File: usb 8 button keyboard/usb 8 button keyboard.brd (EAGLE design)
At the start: 108.5 x 37.8 mm, 31 parts, among them Q1 MMBT2222A, U1 ATMEGA32U4-AU, Y1 16MHZ

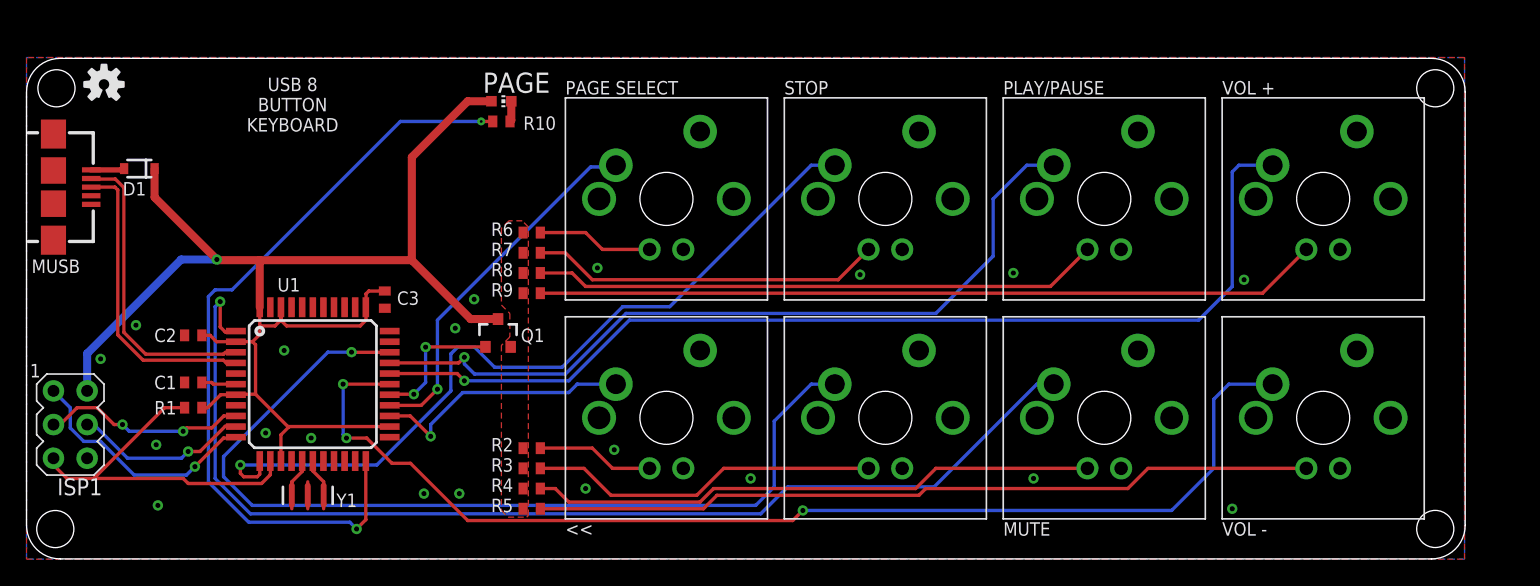
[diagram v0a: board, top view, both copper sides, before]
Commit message: add pcb with proper key spacing.
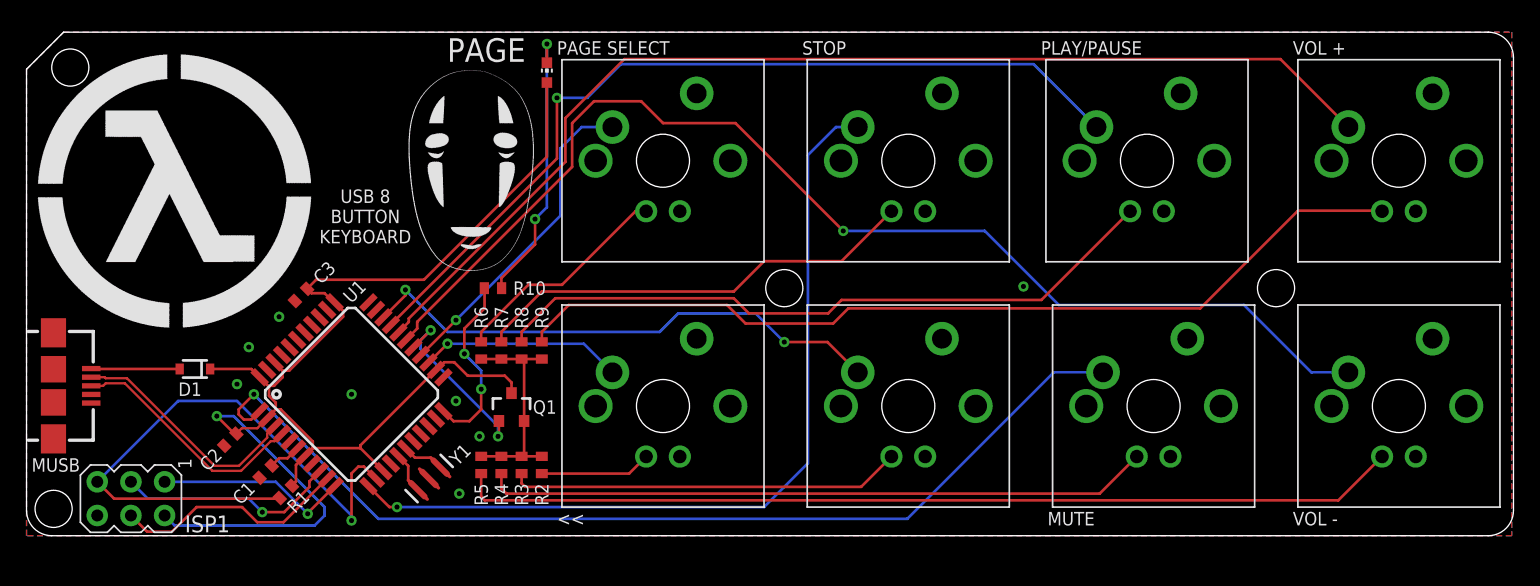
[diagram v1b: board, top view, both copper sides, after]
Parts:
- removed U$15: CPC1-3, cheeper:CPC1-3
- removed U$16: (no value), cheeper:CPC1-3
- moved U$1 81.4 mm to (80.7, 2.11), flipped to the bottom
- moved D1 15.7 mm to (12.7, 12.6)
- moved MUSB 15.0 mm to (2.03, 11.3)
- moved R10 12.6 mm to (35.2, 18.7)
- moved R6 9.67 mm to (34.3, 14.0), turned to 270 degrees
- moved R1 9.44 mm to (19.6, 3.30), turned to 225 degrees
- moved Y1 9.23 mm to (30.4, 4.32), turned to 225 degrees
- moved C1 8.67 mm to (18.0, 4.83), turned to 225 degrees
- moved C2 8.36 mm to (15.4, 7.24), turned to 225 degrees
- moved R7 7.71 mm to (35.8, 14.0), turned to 270 degrees
- moved ISP1 7.22 mm to (7.87, 2.79), turned to 270 degrees
- moved U$10 6.39 mm to (103.5, 28.3)
- moved C3 6.33 mm to (20.7, 18.2), turned to 225 degrees
- moved R8 5.89 mm to (37.3, 14.0), turned to 270 degrees
- moved U$9 5.78 mm to (103.5, 9.78)
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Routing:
- net PLED: track 58.9 -> 13.8 mm
- net SW1: track 71.0 -> 40.6 mm, vias 1 -> 2
- net N$3: track 1.57 -> 21.3 mm, vias 0 -> 2
- net RST: track 27.8 -> 45.9 mm, vias 0 -> 1
- net BL: track 0.00 -> 16.6 mm
- net N$11: track 59.0 -> 71.2 mm
- net N$15: track 59.1 -> 69.1 mm
- net SW2: track 85.2 -> 76.5 mm
- net N$14: track 42.8 -> 51.4 mm
- net N$12: track 8.77 -> 17.0 mm
- net N$10: track 42.7 -> 50.4 mm
- net N$13: track 26.5 -> 33.9 mm
- net SW5: track 60.1 -> 66.0 mm
- net SW4: track 78.6 -> 84.4 mm, vias 1 -> 0
- net D_N: track 22.9 -> 18.0 mm
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- removed copper zone on layer 1, net BL
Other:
- board size 108.5 x 37.8 mm -> 112.1 x 38 mm
- board text added: "C:/Users/Scott/Downloads/oZZuh.bmp"

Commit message: should be the right size now.
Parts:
- moved U$1 79.1 mm to (2.16, 11.3), turned to 270 degrees
- moved U$10 1.58 mm to (105.0, 28.8)
- moved U$11 1.58 mm to (86.0, 28.8)
- moved U$9 1.50 mm to (105.0, 9.78)
- moved U$8 1.00 mm to (86.0, 9.78)
- moved U$12 0.71 mm to (67.0, 28.8)
- moved U$13 0.50 mm to (48.0, 28.8)
- moved U$7 0.50 mm to (67.0, 9.78)
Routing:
- net SW3: track 89.2 -> 91.2 mm
- net N$14: track 51.4 -> 53.1 mm
- net SW6: track 63.0 -> 64.7 mm
- net N$15: track 69.1 -> 70.7 mm
- net N$11: track 71.2 -> 72.7 mm
- net SW5: track 66.0 -> 67.3 mm
- net SW4: track 84.4 -> 85.7 mm
- net SW2: track 76.5 -> 77.5 mm
- net N$10: track 50.4 -> 51.4 mm
- net N$13: track 33.9 -> 34.7 mm
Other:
- board size 112.1 x 38 mm -> 113.3 x 38 mm
- board text removed: "C:/Users/Scott/Downloads/oZZuh.bmp"

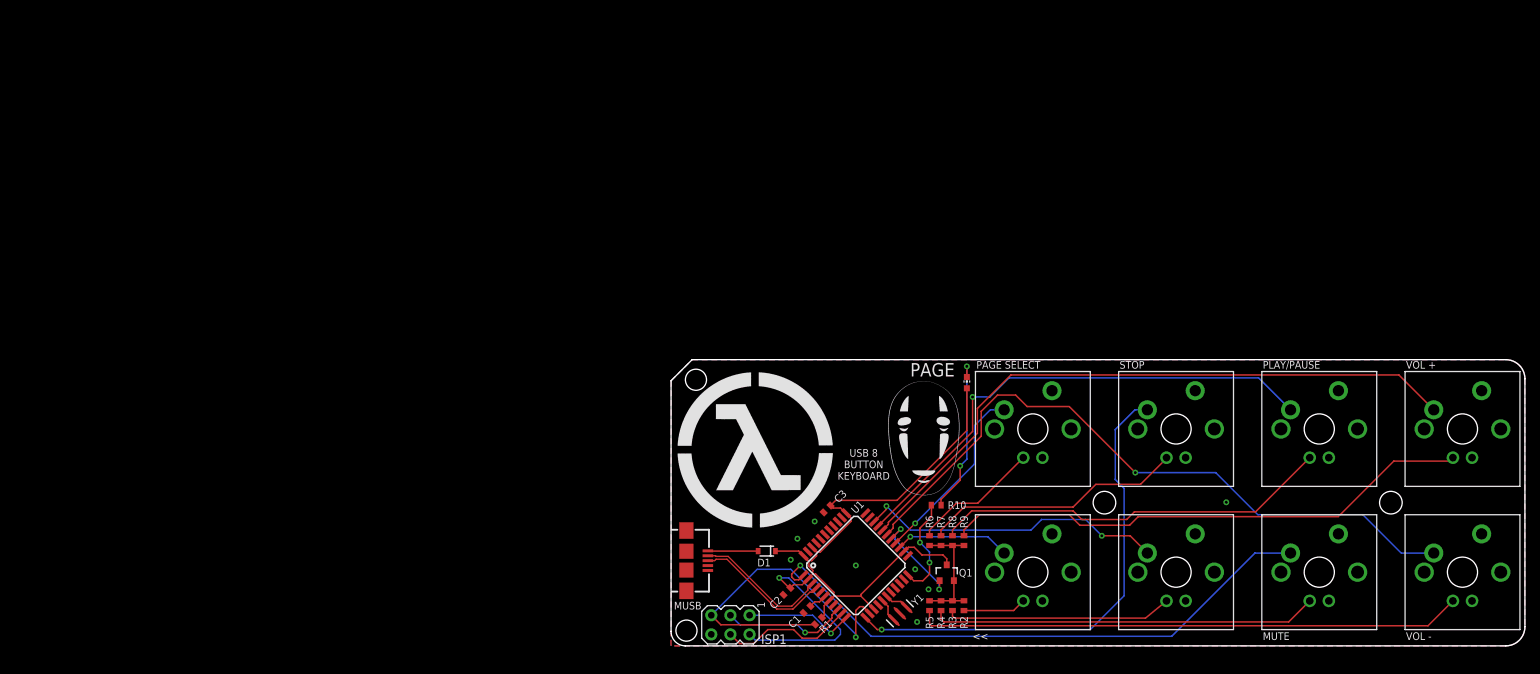
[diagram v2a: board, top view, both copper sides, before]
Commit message: new version. 9 buttons!
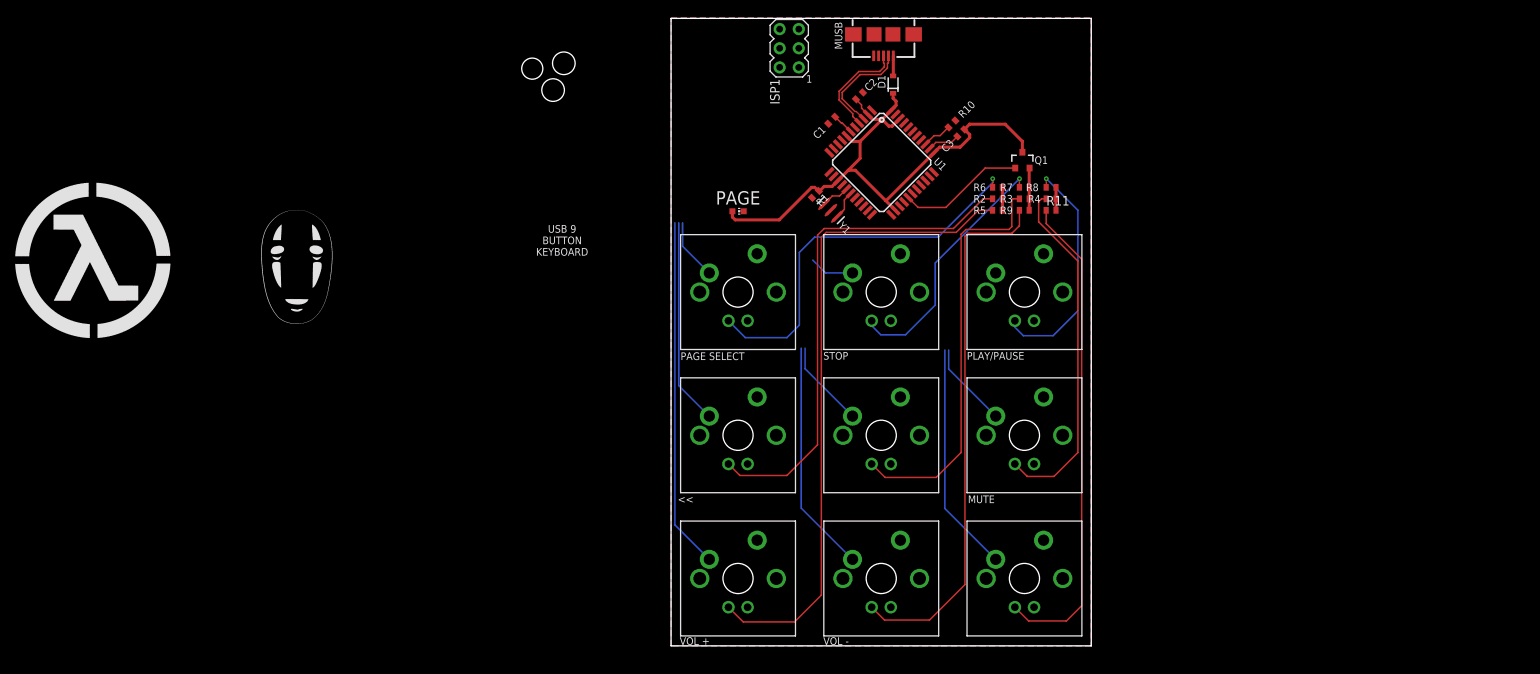
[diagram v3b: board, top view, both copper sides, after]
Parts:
- added R11: 100, cheeper:R0402
- added U$15: CHERRY-MX-LED, cherrymx:CHERRY-MX-LED
- moved U$9 96.1 mm to (8.88, 8.94)
- moved U$10 79.6 mm to (27.9, 8.94)
- moved ISP1 76.9 mm to (15.7, 79.3), turned to 180 degrees
- moved MUSB 74.6 mm to (28.2, 81.1), turned to 270 degrees
- moved U$1 74.4 mm to (28.2, 81.0), turned to 0 degrees
- moved C2 66.4 mm to (25.0, 73.0), turned to 45 degrees
- moved C1 65.0 mm to (21.3, 69.7)
- moved D1 64.1 mm to (29.5, 74.5), turned to 90 degrees
- moved R1 56.6 mm to (19.2, 59.9)
- moved R4 55.9 mm to (50.4, 59.3), turned to 0 degrees
- moved Q1 55.6 mm to (46.6, 64.4)
- moved R3 54.8 mm to (46.9, 59.3), turned to 0 degrees
- moved Y1 54.3 mm to (21.2, 57.8), turned to 135 degrees
- moved R2 54.2 mm to (43.3, 59.3), turned to 0 degrees
- moved U1 53.6 mm to (27.9, 64.1), turned to 315 degrees
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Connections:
- new net N$4: R11.1, U$15.LED1
- new net SW8: U$15.SW1, U1.32
- net BL: now also R11.2
- net GND: now also U$15.LED2, U$15.SW2
- net PLED: now also U1.36; no longer U1.22
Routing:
- net SW5: track 67.3 -> 0.00 mm, vias 1 -> 0
- net SW2: track 77.5 -> 11.4 mm, vias 1 -> 0
- net N$4: track 0.00 -> 64.9 mm
- net N$5: track 8.40 -> 67.2 mm
- net SW6: track 64.7 -> 5.98 mm, vias 1 -> 0
- net SW4: track 85.7 -> 30.8 mm
- net RST: track 45.9 -> 0.00 mm, vias 1 -> 0
- net SW3: track 91.2 -> 46.5 mm, vias 1 -> 0
- net N$12: track 17.2 -> 51.8 mm, vias 0 -> 1
- net SW8: track 0.00 -> 30.6 mm
- net VCC5V: track 107.4 -> 77.3 mm, vias 1 -> 0
- net SW1: track 41.1 -> 11.6 mm, vias 2 -> 0
- net N$9: track 30.1 -> 54.7 mm
- net N$14: track 53.1 -> 31.5 mm, vias 0 -> 1
- net N$3: track 21.3 -> 0.00 mm, vias 2 -> 0
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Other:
- board size 113.3 x 38 mm -> 55.8 x 83.2 mm
- board text added: "USB 9 BUTTON KEYBOARD"
- board text removed: "USB 8 BUTTON KEYBOARD"

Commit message: cleaned up silk, rotated mx switches so LED's are on top, cleaned up some redundent ass routing. added ROHS cert logo.
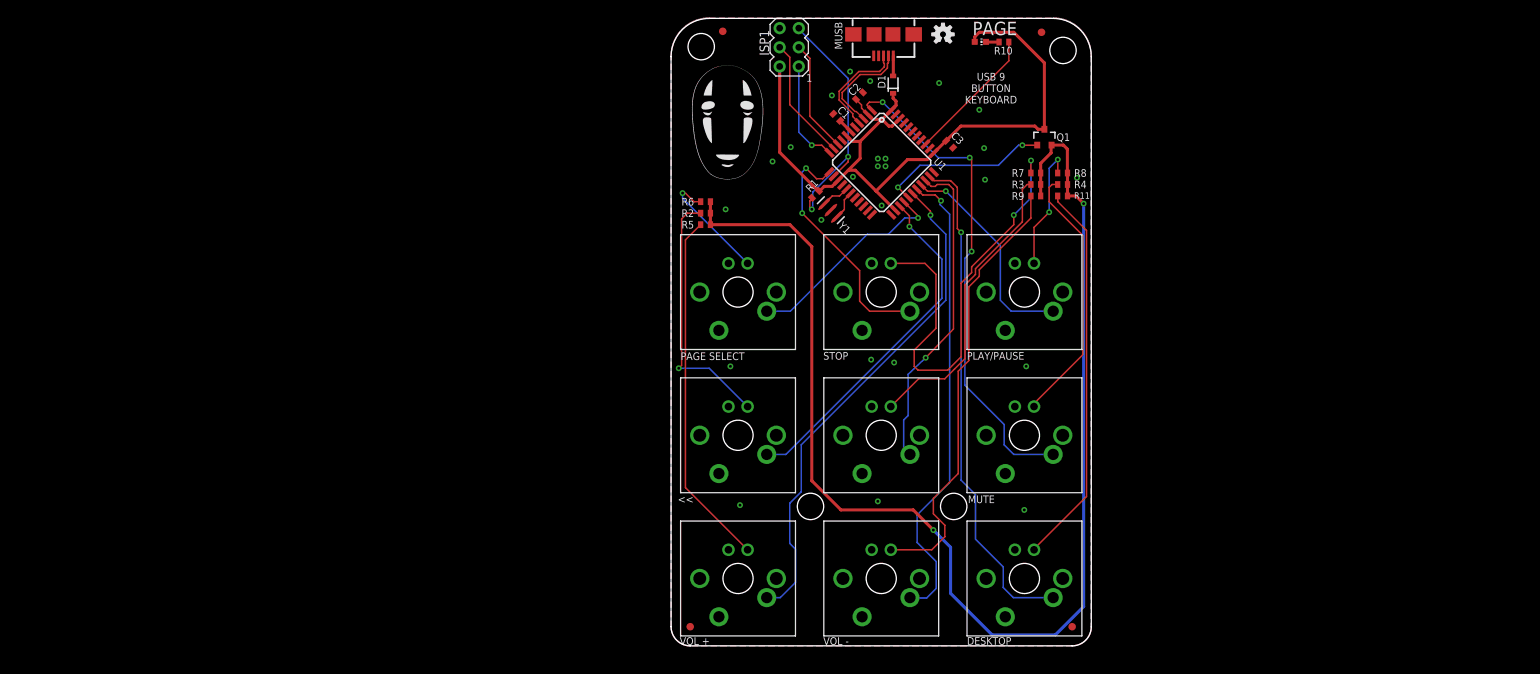
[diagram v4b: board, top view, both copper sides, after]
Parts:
- added FD1, FD2, FD3, FD4: FIDUCIAL, ChipTestJig:FIDUCIAL_1MM
- added U$16: (no value), SparkFun-Aesthetics:OSHW-LOGO-S
- added U$17: (no value), SparkFun-Aesthetics:ROHS_LOGO_0.18_IN
- moved PAGE 39.2 mm to (41.0, 80.1)
- moved R2 38.8 mm to (4.57, 57.4)
- moved R5 38.8 mm to (4.57, 55.9)
- moved R6 38.8 mm to (4.57, 58.9)
- moved R10 12.9 mm to (44.2, 80.1), turned to 180 degrees
- moved Q1 4.22 mm to (49.5, 67.4)
- moved R11 2.44 mm to (51.9, 59.7)
- moved R3 2.44 mm to (48.4, 61.2)
- moved R4 2.44 mm to (51.9, 61.2)
- moved R7 2.44 mm to (48.4, 62.7)
- moved R8 2.44 mm to (51.9, 62.7)
- moved R9 2.44 mm to (48.4, 59.7)
- moved C3 2.11 mm to (37.0, 66.5), turned to 315 degrees
- moved C1 0.77 mm to (22.0, 70.1), turned to 135 degrees
- moved ISP1 0.13 mm to (15.7, 79.4)
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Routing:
- net BL: track 11.7 -> 170.4 mm, vias 0 -> 2
- net SW2: track 11.4 -> 65.6 mm, vias 0 -> 3
- net N$11: track 86.3 -> 47.4 mm
- net SW8: track 30.6 -> 67.1 mm, vias 0 -> 1
- net N$12: track 51.8 -> 15.8 mm
- net RST: track 0.00 -> 33.9 mm, vias 0 -> 2
- net N$5: track 67.2 -> 34.1 mm, vias 0 -> 1
- net SW4: track 30.8 -> 62.7 mm, vias 0 -> 1
- net SW1: track 11.6 -> 42.7 mm, vias 0 -> 1
- net SW5: track 0.00 -> 28.7 mm, vias 0 -> 1
- net SW6: track 5.98 -> 32.4 mm, vias 0 -> 2
- net VCC5V: track 77.3 -> 102.4 mm
- net N$13: track 33.8 -> 58.7 mm, vias 1 -> 2
- net SW3: track 46.5 -> 67.0 mm, vias 0 -> 1
- net SW7: track 8.13 -> 28.1 mm, vias 0 -> 1
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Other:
- outline, holes or cut-outs redrawn
- board text added: "ALLEEYBEACHELECTRIC@GMAIL.COM"
- board text added: "DESKTOP"
- board text removed: "SCOTT@NEXTTHING.CO"
